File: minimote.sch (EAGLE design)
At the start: 41 parts, among them IC1 ATTINY441/841-SSU, J1 AVR_SPI_PROG_3X2PTH

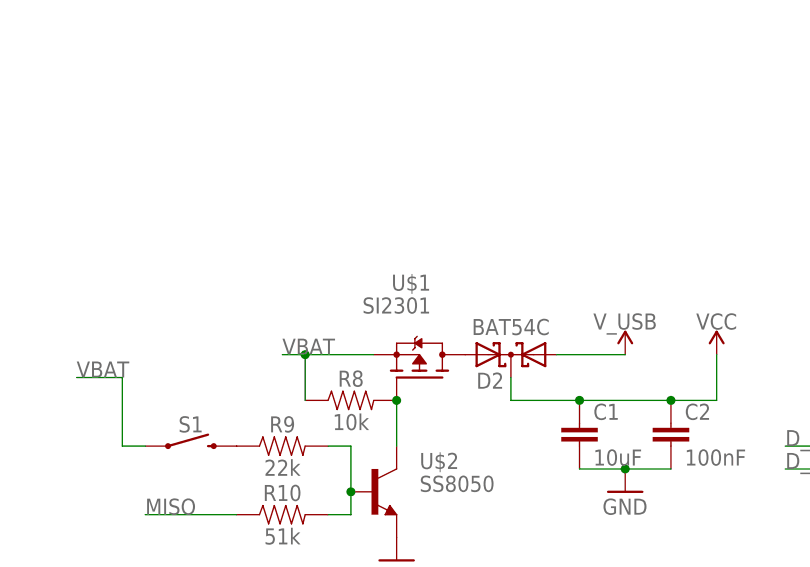
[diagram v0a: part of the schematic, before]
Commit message: cleaned up ground traces
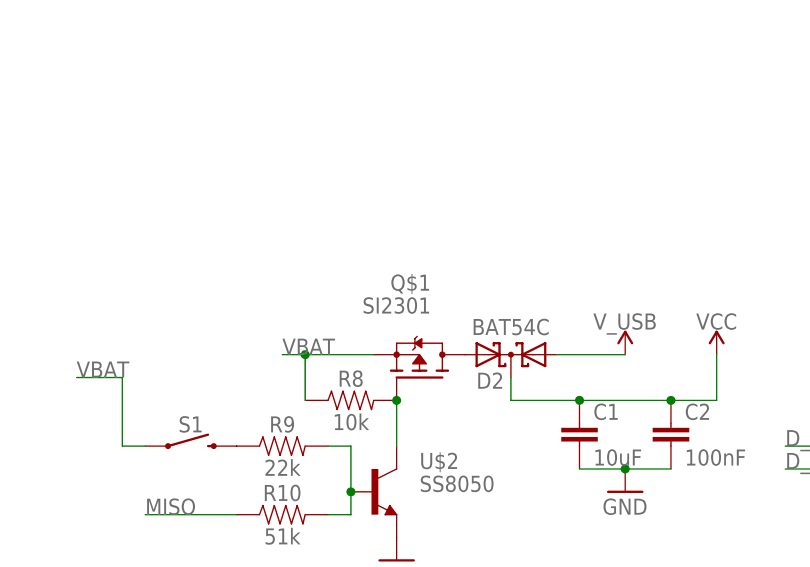
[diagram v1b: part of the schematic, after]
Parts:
- renumbered U$1 to Q$1
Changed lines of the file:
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@@
 <part name="SUPPLY4" library="SparkFun-PowerSymbols" library_urn="urn:adsk.eagle:library:530" deviceset="V_USB" device=""/>
 <part name="FRAME1" library="SparkFun-Aesthetics" library_urn="urn:adsk.eagle:library:507" deviceset="FRAME-LEDGER" device="" package3d_urn="urn:adsk.eagle:package:37121/1"/>
-<part name="U$1" library="minimote" deviceset="SI2301" device=""/>
+<part name="Q$1" library="minimote" deviceset="SI2301" device=""/>
 <part name="R8" library="SparkFun-Resistors" library_urn="urn:adsk.eagle:library:532" deviceset="3.3KOHM" device="-0603-1/10W-1%" package3d_urn="urn:adsk.eagle:package:39650/1" value="10k"/>
 <part name="SUPPLY5" library="SparkFun-PowerSymbols" library_urn="urn:adsk.eagle:library:530" deviceset="V_USB" device=""/>
@@
 <instance part="FRAME1" gate="G$1" x="-40.64" y="-40.64"/>
 <instance part="FRAME1" gate="G$2" x="289.56" y="-40.64"/>
-<instance part="U$1" gate="G$1" x="20.32" y="83.82" smashed="yes" rot="R90">
+<instance part="Q$1" gate="G$1" x="20.32" y="83.82" smashed="yes" rot="R90">
 <attribute name="VALUE" x="21.59" y="92.71" size="1.778" layer="96" rot="R180"/>
 <attribute name="NAME" x="21.59" y="95.25" size="1.778" layer="95" rot="R180"/>
@@
 <segment>
 <wire x1="5.08" y1="86.36" x2="7.62" y2="86.36" width="0.1524" layer="91"/>
-<pinref part="U$1" gate="G$1" pin="S"/>
+<pinref part="Q$1" gate="G$1" pin="S"/>
 <label x="5.08" y="86.36" size="1.778" layer="95"/>
 <pinref part="R8" gate="G$1" pin="1"/>
@@
 <net name="N$4" class="0">
 <segment>
-<pinref part="U$1" gate="G$1" pin="G"/>
+<pinref part="Q$1" gate="G$1" pin="G"/>
 <pinref part="R8" gate="G$1" pin="2"/>
 <pinref part="U$2" gate="G$1" pin="C"/>
@@
 <net name="N$5" class="0">
 <segment>
-<pinref part="U$1" gate="G$1" pin="D"/>
+<pinref part="Q$1" gate="G$1" pin="D"/>
 <pinref part="D2" gate="G$1" pin="A2"/>
 </segment>

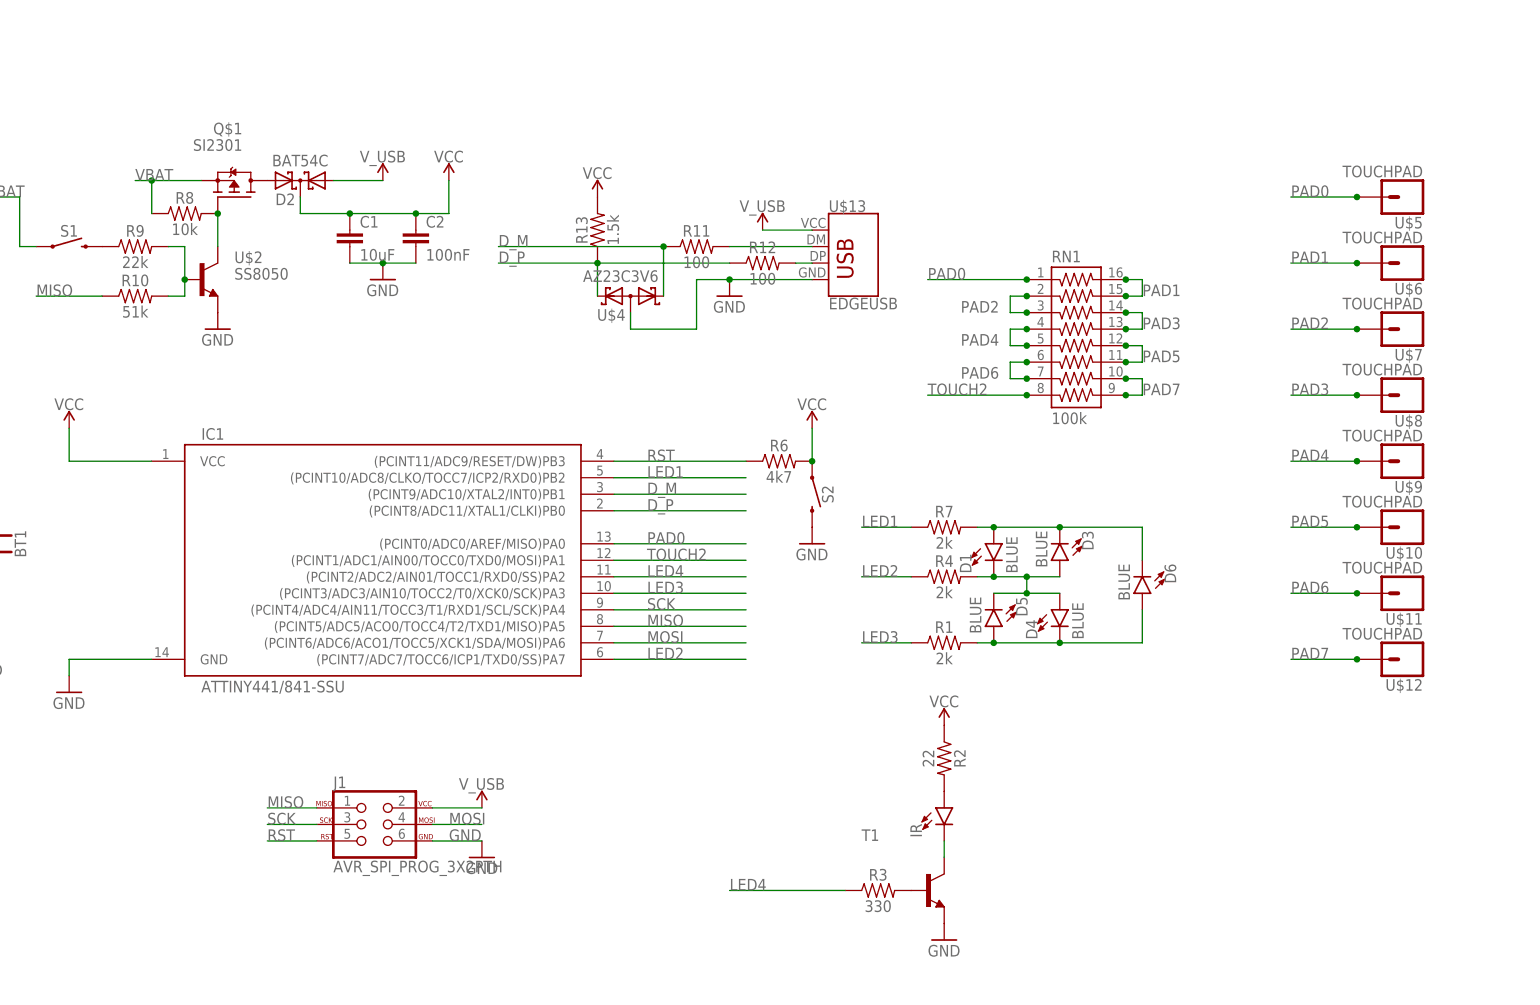
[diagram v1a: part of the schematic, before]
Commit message: Cleaned up silkscreen
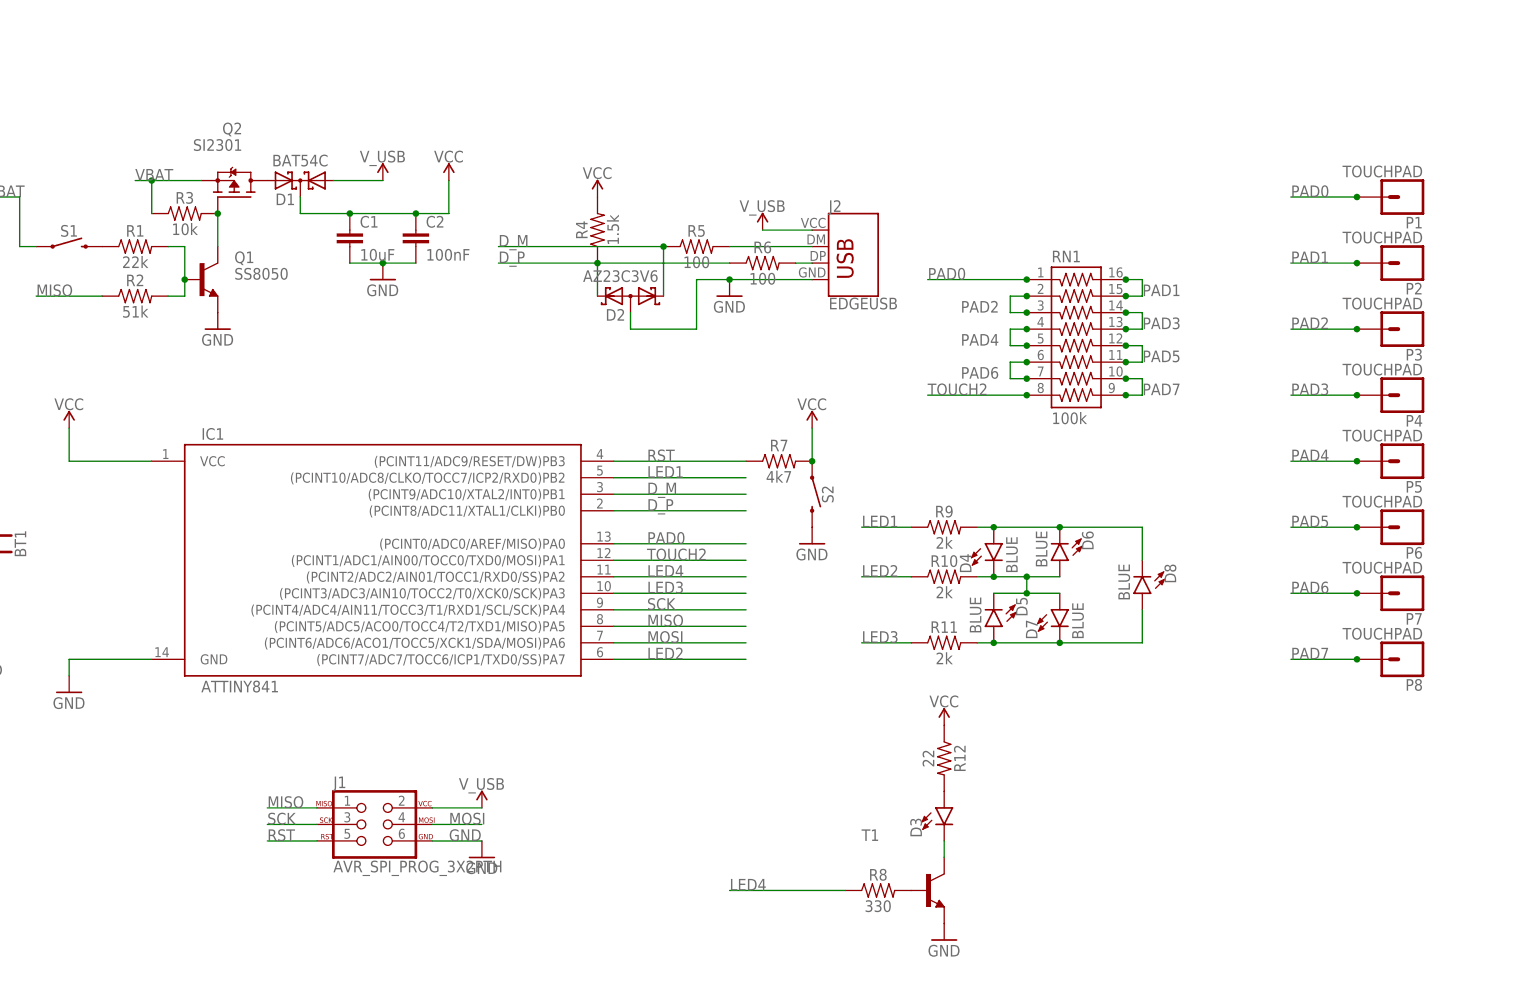
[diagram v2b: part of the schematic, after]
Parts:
- removed IR: (no value), SparkFun-LED:LED3MM
- removed Q$1: SI2301, minimote:SI2301
- removed R13: 1.5k, SparkFun-Resistors:3.3KOHM-0603-1/10W-1%
- removed U$10, U$11, U$12, U$5, U$6, U$7, U$8, U$9: TOUCHPAD, minimote:TOUCHPAD
- removed U$13: EDGEUSB, minimote:EDGEUSB
- removed U$2: SS8050, minimote:SS8050
- removed U$4: AZ23C3V6, minimote:AZ23C3V6
- added D7, D8: BLUE, SparkFun-LED:LED-BLUE0603
- added J2: EDGEUSB, minimote:EDGEUSB
- added P1, P2, P3, P4, P5, P6, P7, P8: TOUCHPAD, minimote:TOUCHPAD
- added Q1: SS8050, minimote:SS8050
- added Q2: SI2301, minimote:SI2301
- added R5: 100, SparkFun-Resistors:3.3KOHM-0603-1/10W-1%
- D1: value BLUE -> BAT54C; device SparkFun-LED:LED-BLUE0603 -> diode:BAT54C
- D2: value BAT54C -> AZ23C3V6; device diode:BAT54C -> minimote:AZ23C3V6
- D3: value BLUE -> (none); device SparkFun-LED:LED-BLUE0603 -> SparkFun-LED:LED3MM
- IC1: value ATTINY441/841-SSU -> ATTINY841
- R1: value 2k -> 22k
- R10: value 51k -> 2k
- R11: value 100 -> 2k
- R12: value 100 -> 22
- R2: value 22 -> 51k
- R3: value 330 -> 10k
- R4: value 2k -> 1.5k
- R6: value 4k7 -> 100
- R7: value 2k -> 4k7
- R8: value 10k -> 330
- R9: value 22k -> 2k
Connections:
- net D_M: now also D2.K1, R5.1; no longer R11.1, U$4.K1
- net D_P: now also D2.K2, R4.1, R6.1; no longer R12.1, R13.1, U$4.K2
- net GND: now also D2.AA, J2.GND, Q1.E; no longer U$13.GND, U$2.E, U$4.AA
- net LED1: now also R9.1; no longer R7.1
- net LED2: now also R10.1; no longer R4.1
- net LED3: now also R11.1; no longer R1.1
- net LED4: now also R8.1; no longer R3.1
- net MISO: now also R2.1; no longer R10.1
- net N$1: now also D3.A, R12.2; no longer IR.A, R2.2
- net N$123: now also D7.C, D8.A, R11.2; no longer D4.C, D6.A, R1.2
- net N$124: now also D4.C, D6.A, D7.A, R10.2; no longer D1.C, D3.A, D4.A, R4.2
- net N$125: now also D4.A, D8.C, R9.2; no longer D1.A, D3.C, R7.2
- net N$2: now also D3.C; no longer IR.C
- net N$3: now also R8.2; no longer R3.2
- net N$4: now also Q1.C, Q2.G, R3.2; no longer Q$1.G, R8.2, U$2.C
- net N$5: now also D1.A2, Q2.D; no longer D2.A2, Q$1.D
- net N$6: now also Q1.B, R1.2, R2.2; no longer R10.2, R9.2, U$2.B
- net N$7: now also R1.1; no longer R9.1
- net N$8: now also J2.D-, R5.2; no longer R11.2, U$13.D-
- net N$9: now also J2.D+, R6.2; no longer R12.2, U$13.D+
- net PAD0: now also P1.1; no longer U$5.1
- net PAD1: now also P2.1; no longer U$6.1
- net PAD2: now also P3.1; no longer U$7.1
- net PAD3: now also P4.1; no longer U$8.1
- net PAD4: now also P5.1; no longer U$9.1
- net PAD5: now also P6.1; no longer U$10.1
- net PAD6: now also P7.1; no longer U$11.1
- net PAD7: now also P8.1; no longer U$12.1
- net RST: now also R7.1; no longer R6.1
- net VBAT: now also Q2.S, R3.1; no longer Q$1.S, R8.1
- net VCC: now also D1.CC, R12.1, R4.2, R7.2; no longer D2.CC, R13.2, R2.1, R6.2
- net V_USB: now also D1.A1, J2.VBUS; no longer D2.A1, U$13.VBUS
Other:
- moved on the sheet: D3, D4, D6, R1, R10, R11, R12, R2, R3, R4, R6, R7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

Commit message: Version submitted to DirtyPCBs
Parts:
- D3: device SparkFun-LED:LED3MM -> minimote:LED3MM
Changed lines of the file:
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@@
 <part name="IC1" library="bt_avr" deviceset="ATTINY441/841" device="-SSU" value="ATTINY841"/>
 <part name="GND2" library="supply1" library_urn="urn:adsk.eagle:library:371" deviceset="GND" device=""/>
-<part name="D3" library="SparkFun-LED" deviceset="LED" device="3MM"/>
 <part name="GND1" library="supply1" library_urn="urn:adsk.eagle:library:371" deviceset="GND" device=""/>
 <part name="GND5" library="supply1" library_urn="urn:adsk.eagle:library:371" deviceset="GND" device=""/>
@@
 <part name="D2" library="minimote" deviceset="AZ23C3V6" device=""/>
 <part name="T1" library="transistor" library_urn="urn:adsk.eagle:library:402" deviceset="*-NPN-" device="SOT23-BEC" package3d_urn="urn:adsk.eagle:package:29919/2" technology="MMBT3904LT1"/>
+<part name="D3" library="minimote" deviceset="LED" device="3MM"/>
 </parts>
 <sheets>
@@
 <instance part="IC1" gate="IC1" x="43.18" y="27.94"/>
 <instance part="GND2" gate="1" x="-5.08" y="7.62"/>
-<instance part="D3" gate="G$1" x="129.54" y="-10.16"/>
 <instance part="GND1" gate="1" x="-17.78" y="12.7"/>
 <instance part="GND5" gate="1" x="58.42" y="-17.78"/>
@@
 <instance part="D2" gate="D$1" x="81.28" y="68.58" rot="R180"/>
 <instance part="T1" gate="G$1" x="127" y="-22.86"/>
+<instance part="D3" gate="G$1" x="129.54" y="-10.16"/>
 </instances>
 <busses>
@@
 <net name="N$2" class="0">
 <segment>
-<pinref part="D3" gate="G$1" pin="C"/>
 <wire x1="129.54" y1="-17.78" x2="129.54" y2="-15.24" width="0.1524" layer="91"/>
 <pinref part="T1" gate="G$1" pin="C"/>
-</segment>
-</net>
-<net name="N$1" class="0">
-<segment>
-<pinref part="D3" gate="G$1" pin="A"/>
-<pinref part="R12" gate="G$1" pin="2"/>
+<pinref part="D3" gate="G$1" pin="C"/>
 </segment>
 </net>
@@
 </segment>
 </net>
+<net name="N$1" class="0">
+<segment>
+<pinref part="R12" gate="G$1" pin="2"/>
+<pinref part="D3" gate="G$1" pin="A"/>
+</segment>
+</net>

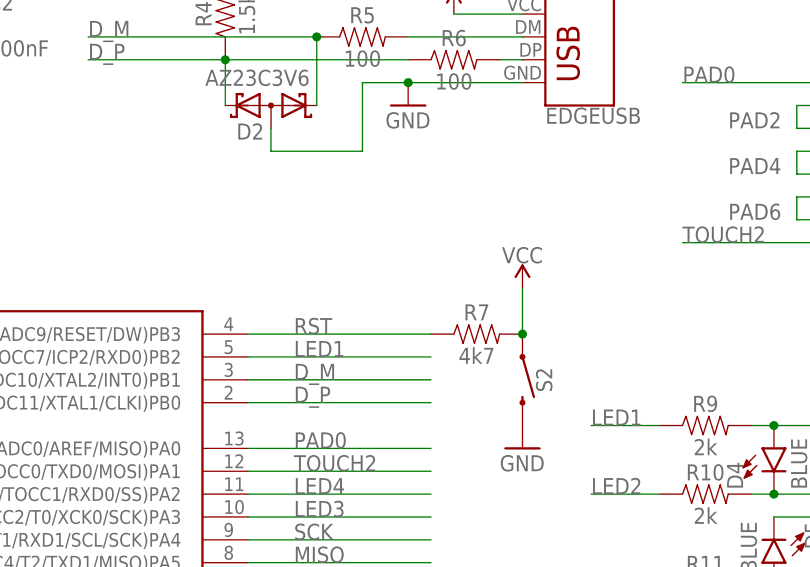
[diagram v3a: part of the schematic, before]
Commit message: fixed pwr ground short
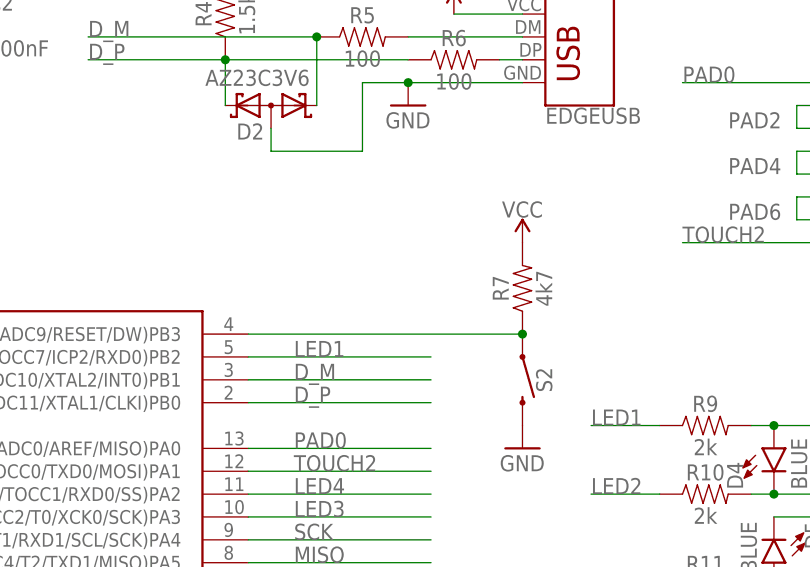
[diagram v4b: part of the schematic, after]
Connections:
- new net N$10: IC1.(PCINT11/ADC9/RESET/DW)PB3, R7.1, S2.1
- net RST: no longer IC1.(PCINT11/ADC9/RESET/DW)PB3, R7.1
- net VCC: no longer S2.1
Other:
- moved on the sheet: R7
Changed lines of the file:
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@@
 <instance part="R8" gate="G$1" x="119.38" y="-22.86"/>
 <instance part="R12" gate="G$1" x="129.54" y="-2.54" rot="R270"/>
-<instance part="R7" gate="G$1" x="104.14" y="43.18"/>
+<instance part="R7" gate="G$1" x="109.22" y="48.26" rot="R90"/>
 <instance part="D4" gate="G$1" x="137.16" y="30.48"/>
 <instance part="D6" gate="G$1" x="147.32" y="27.94" rot="R180"/>
@@
 <instance part="J1" gate="G$1" x="40.64" y="-12.7"/>
 <instance part="SUPPLY1" gate="G$1" x="-5.08" y="48.26"/>
-<instance part="SUPPLY7" gate="G$1" x="109.22" y="48.26"/>
+<instance part="SUPPLY7" gate="G$1" x="109.22" y="53.34"/>
 <instance part="SUPPLY8" gate="G$1" x="129.54" y="2.54"/>
 <instance part="R11" gate="G$1" x="129.54" y="15.24"/>
@@
 </segment>
 <segment>
-<wire x1="109.22" y1="48.26" x2="109.22" y2="43.18" width="0.1524" layer="91"/>
-<pinref part="R7" gate="G$1" pin="2"/>
-<pinref part="S2" gate="G$1" pin="1"/>
-<junction x="109.22" y="43.18"/>
-<pinref part="SUPPLY7" gate="G$1" pin="VCC"/>
-</segment>
-<segment>
 <pinref part="R12" gate="G$1" pin="1"/>
 <pinref part="SUPPLY8" gate="G$1" pin="VCC"/>
@@
 <pinref part="SUPPLY5" gate="G$1" pin="VCC"/>
 </segment>
+<segment>
+<pinref part="SUPPLY7" gate="G$1" pin="VCC"/>
+<pinref part="R7" gate="G$1" pin="2"/>
+</segment>
 </net>
 <net name="RST" class="0">
-<segment>
-<pinref part="IC1" gate="IC1" pin="(PCINT11/ADC9/RESET/DW)PB3"/>
-<wire x1="78.74" y1="43.18" x2="99.06" y2="43.18" width="0.1524" layer="91"/>
-<label x="83.82" y="43.18" size="1.778" layer="95"/>
-<pinref part="R7" gate="G$1" pin="1"/>
-</segment>
 <segment>
 <wire x1="25.4" y1="-15.24" x2="33.02" y2="-15.24" width="0.1524" layer="91"/>
@@
 </segment>
 </net>
+<net name="N$10" class="0">
+<segment>
+<pinref part="S2" gate="G$1" pin="1"/>
+<pinref part="R7" gate="G$1" pin="1"/>
+<pinref part="IC1" gate="IC1" pin="(PCINT11/ADC9/RESET/DW)PB3"/>
+<wire x1="78.74" y1="43.18" x2="109.22" y2="43.18" width="0.1524" layer="91"/>
+<junction x="109.22" y="43.18"/>
+</segment>
+</net>
